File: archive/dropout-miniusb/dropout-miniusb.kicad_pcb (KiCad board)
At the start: 2 copper layers, 75.1 x 94.2 mm, 47 parts, among them SW1 Rotary_Encoder_Switch, SW2 SW_Push, U1 ProMicro

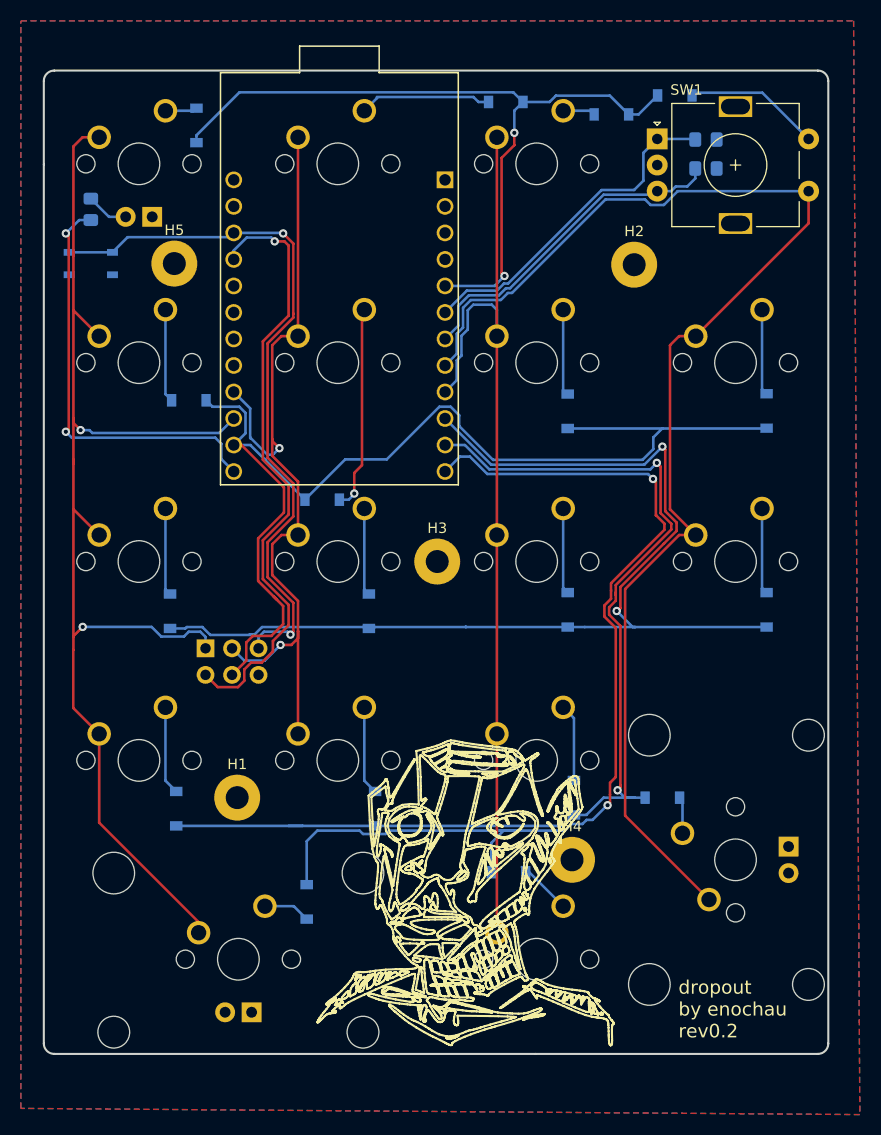
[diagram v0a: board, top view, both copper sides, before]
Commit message: 3 piece panelization
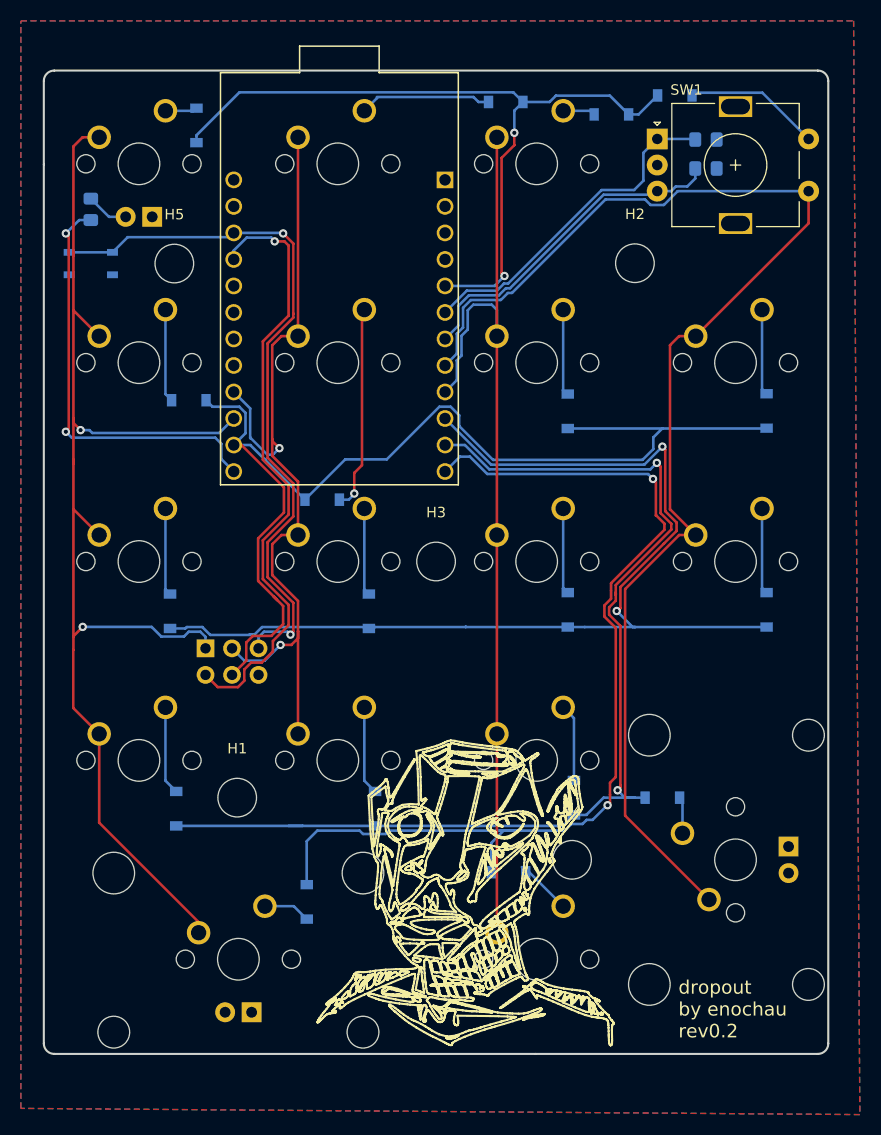
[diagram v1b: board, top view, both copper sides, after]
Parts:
- H1, H2, H3, H4, H5: footprint MountingHole:MountingHole_2.2mm_M2_Pad -> MountingHole:MountingHole_3.7mm
- moved H2 0.16 mm to (194.2, 69.0)
- moved H3 0.11 mm to (175.1, 97.6)
